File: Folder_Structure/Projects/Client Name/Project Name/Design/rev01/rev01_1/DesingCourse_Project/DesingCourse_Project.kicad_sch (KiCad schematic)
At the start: 0 parts

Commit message: Update 6
SCH and LIB for MOSFET page done, missing passive components
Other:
- title: ESC_rev01_1 -> PCB Mastery Project
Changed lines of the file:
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@@
 	(paper "A4")
 	(title_block
-		(title "ESC_rev01_1")
-		(date "2026-01-15")
-		(rev "Rev01")
+		(title "PCB Mastery Project")
+		(date "2026-01-27")
+		(rev "001")
 		(company "Integro Consulting AB")
 		(comment 1 "TBD")

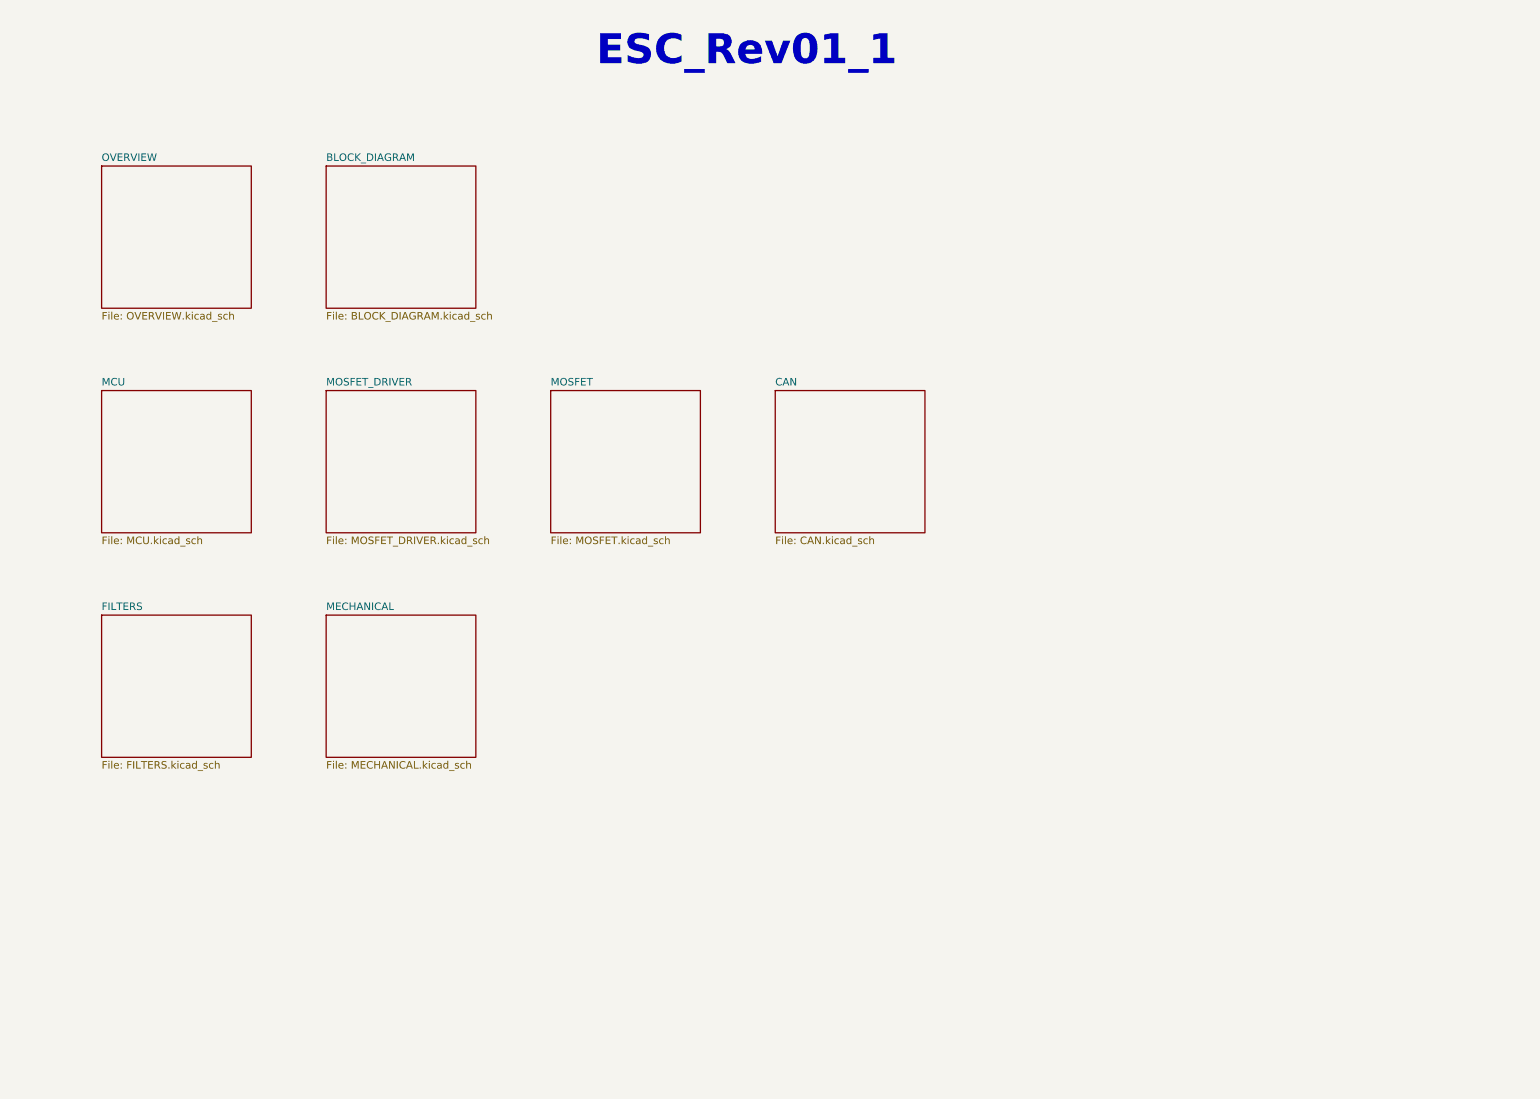
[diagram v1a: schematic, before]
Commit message: Update 8
Page 1 finished, INPUT finished, Start of USB-C
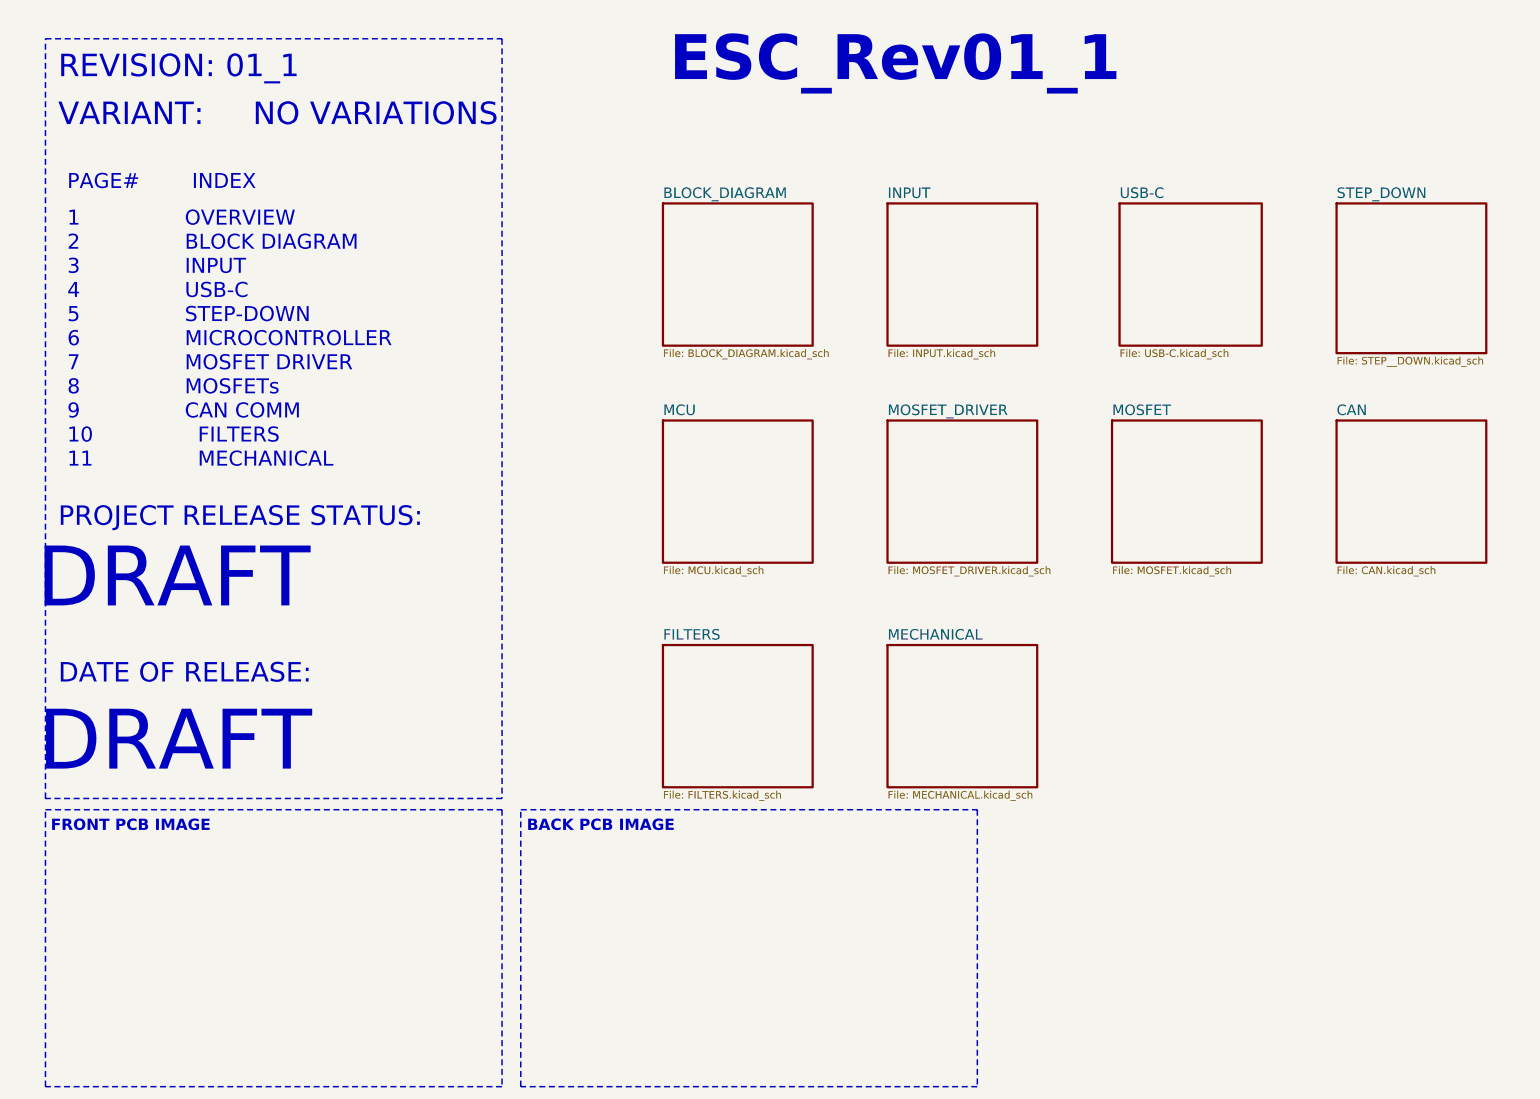
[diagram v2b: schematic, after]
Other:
- removed sheet OVERVIEW
- added sheet INPUT (INPUT.kicad_sch)
- added sheet STEP_DOWN (STEP__DOWN.kicad_sch)
- added sheet USB-C (USB-C.kicad_sch)
- note added: "1 OVERVIEW 2 BLOCK DIAGRAM 3 INPUT 4 USB-C 5 STEP-DOWN 6 MICROCONTROLLER 7 MOSFET DRIVER 8 MOSFETs 9 CAN COMM 10 FILTERS 11 MECHANICAL"
- note added: "BACK PCB IMAGE"
- note added: "DRAFT"
- note added: "FRONT PCB IMAGE"
- note added: "NO VARIATIONS"
- note added: "PAGE# INDEX"
- note added: "PROJECT RELEASE STATUS: DATE OF RELEASE:"
- note added: "REVISION: ${REVISION}"
- note added: "VARIANT:"
